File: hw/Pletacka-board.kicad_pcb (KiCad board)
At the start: 2 copper layers, 12 parts, among them SW1 SW_Push_Dual_x2, SW2 SW_Push_Dual_x2, SW3 SW_Push_Dual_x2

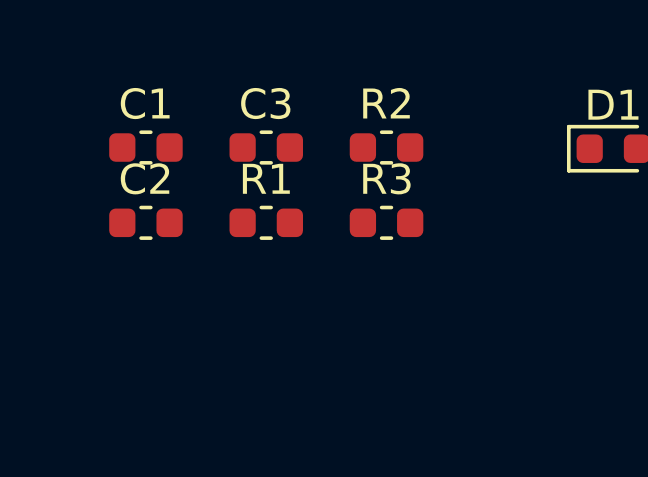
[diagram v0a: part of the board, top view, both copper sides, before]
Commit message: Add octocoupler library
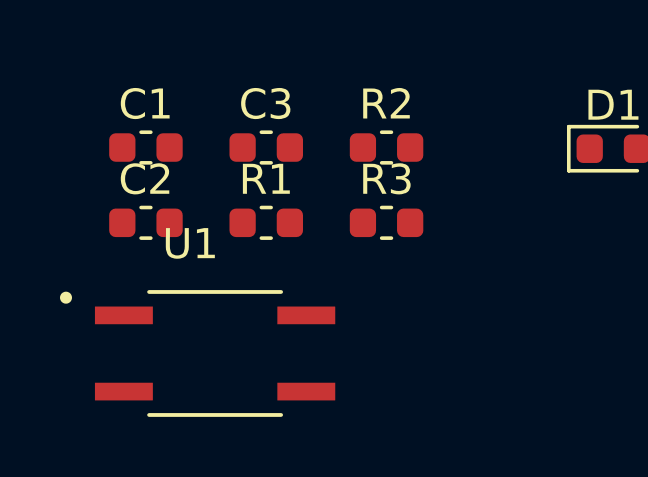
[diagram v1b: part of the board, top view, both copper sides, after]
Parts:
- added U1: EL357N(A)(TA)-G, EL357N_A__TA_-G:SOP254P700X200-4N, F.Cu at (-304.8, -236.2)
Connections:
- E1 pad 12: (no net) -> Net-(E1-Pad12)
- E1 pad 13: (no net) -> Net-(E1-Pad13)
- E1 pad 15: (no net) -> Net-(E1-Pad15)
- E1 pad 17: (no net) -> Net-(E1-Pad17)
- E1 pad 2: (no net) -> Net-(E1-Pad2)
- E1 pad 21: (no net) -> Net-(E1-Pad21)
- E1 pad 22: (no net) -> Net-(E1-Pad22)
- E1 pad 25: (no net) -> Net-(E1-Pad25)
- E1 pad 26: (no net) -> Net-(E1-Pad26)
- E1 pad 27: (no net) -> Net-(E1-Pad27)
- E1 pad 32: (no net) -> Net-(E1-Pad32)
- E1 pad 33: (no net) -> Net-(E1-Pad33)
- E1 pad 36: (no net) -> Net-(E1-Pad36)
- E1 pad 37: (no net) -> Net-(E1-Pad37)
- E1 pad 38: (no net) -> Net-(E1-Pad38)
- E1 pad 39: (no net) -> Net-(E1-Pad39)
- E1 pad 5V: (no net) -> +5V
- R1 pad 1: (no net) -> BTN_RESET
- R2 pad 1: (no net) -> BTN_1
- R3 pad 1: (no net) -> BTN_2
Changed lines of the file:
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@@
     (tracks 0)
     (zones 0)
-    (modules 12)
-    (nets 7)
+    (modules 13)
+    (nets 31)
   )
   (page A4)
@@
   (net 5 "Net-(C2-Pad1)")
   (net 6 "Net-(D1-Pad2)")
+  (net 7 "Net-(E1-Pad12)")
+  (net 8 "Net-(E1-Pad13)")
+  (net 9 "Net-(E1-Pad15)")
+  (net 10 "Net-(E1-Pad2)")
+  (net 11 "Net-(E1-Pad17)")
+  (net 12 "Net-(E1-Pad22)")
+  (net 13 "Net-(E1-Pad21)")
+  (net 14 +5V)
+  (net 15 "Net-(E1-Pad27)")
+  (net 16 "Net-(E1-Pad26)")
+  (net 17 "Net-(E1-Pad25)")
+  (net 18 "Net-(E1-Pad33)")
+  (net 19 "Net-(E1-Pad32)")
+  (net 20 "Net-(E1-Pad39)")
+  (net 21 "Net-(E1-Pad38)")
+  (net 22 "Net-(E1-Pad37)")
+  (net 23 "Net-(E1-Pad36)")
+  (net 24 BTN_RESET)
+  (net 25 BTN_1)
+  (net 26 BTN_2)
+  (net 27 "Net-(U1-Pad1)")
+  (net 28 "Net-(U1-Pad2)")
+  (net 29 "Net-(U1-Pad3)")
+  (net 30 "Net-(U1-Pad4)")
   (net_class Default "This is the default net class."
     (clearance 0.2)
@@
     (uvia_drill 0.1)
     (add_net +3V3)
+    (add_net +5V)
     (add_net BTN_1)
     (add_net BTN_2)
+    (add_net BTN_RESET)
     (add_net GND)
     (add_net "Net-(C1-Pad1)")
@@
     (add_net "Net-(C3-Pad1)")
     (add_net "Net-(D1-Pad2)")
+    (add_net "Net-(E1-Pad12)")
+    (add_net "Net-(E1-Pad13)")
+    (add_net "Net-(E1-Pad15)")
+    (add_net "Net-(E1-Pad17)")
+    (add_net "Net-(E1-Pad2)")
+    (add_net "Net-(E1-Pad21)")
+    (add_net "Net-(E1-Pad22)")
+    (add_net "Net-(E1-Pad25)")
+    (add_net "Net-(E1-Pad26)")
+    (add_net "Net-(E1-Pad27)")
+    (add_net "Net-(E1-Pad32)")
+    (add_net "Net-(E1-Pad33)")
+    (add_net "Net-(E1-Pad36)")
+    (add_net "Net-(E1-Pad37)")
+    (add_net "Net-(E1-Pad38)")
+    (add_net "Net-(E1-Pad39)")
+    (add_net "Net-(U1-Pad1)")
+    (add_net "Net-(U1-Pad2)")
+    (add_net "Net-(U1-Pad3)")
+    (add_net "Net-(U1-Pad4)")
+  )
+  (module EL357N_A__TA_-G:SOP254P700X200-4N (layer F.Cu)
+    (at -304.8 -236.22)
+    (fp_text reference U1 (at -0.82154 -3.64071) (layer F.SilkS)
+      (effects (font (size 1.002756 1.002756) (thickness 0.015)))
+    )
+    (fp_text value "EL357N(A)(TA)-G" (at 6.80906 3.64082) (layer F.Fab)
+      (effects (font (size 1.001874 1.001874) (thickness 0.015)))
+    )
+    (fp_circle (center -4.97 -1.86) (end -4.87 -1.86) (layer F.SilkS) (width 0.2))
+    (fp_circle (center -4.97 -1.86) (end -4.87 -1.86) (layer F.Fab) (width 0.2))
+    (fp_line (start -2.2 -2.05) (end 2.2 -2.05) (layer F.Fab) (width 0.127))
+    (fp_line (start -2.2 2.05) (end 2.2 2.05) (layer F.Fab) (width 0.127))
+    (fp_line (start -2.2 -2.05) (end 2.2 -2.05) (layer F.SilkS) (width 0.127))
+    (fp_line (start -2.2 2.05) (end 2.2 2.05) (layer F.SilkS) (width 0.127))
+    (fp_line (start -2.2 -2.05) (end -2.2 2.05) (layer F.Fab) (width 0.127))
+    (fp_line (start 2.2 -2.05) (end 2.2 2.05) (layer F.Fab) (width 0.127))
+    (fp_line (start -4.255 -2.3) (end 4.255 -2.3) (layer F.CrtYd) (width 0.05))
+    (fp_line (start -4.255 2.3) (end 4.255 2.3) (layer F.CrtYd) (width 0.05))
+    (fp_line (start -4.255 -2.3) (end -4.255 2.3) (layer F.CrtYd) (width 0.05))
+    (fp_line (start 4.255 -2.3) (end 4.255 2.3) (layer F.CrtYd) (width 0.05))
+    (pad 1 smd rect (at -3.04 -1.27) (size 1.93 0.59) (layers F.Cu F.Paste F.Mask)
+      (net 27 "Net-(U1-Pad1)"))
+    (pad 2 smd rect (at -3.04 1.27) (size 1.93 0.59) (layers F.Cu F.Paste F.Mask)
+      (net 28 "Net-(U1-Pad2)"))
+    (pad 3 smd rect (at 3.04 1.27) (size 1.93 0.59) (layers F.Cu F.Paste F.Mask)
+      (net 29 "Net-(U1-Pad3)"))
+    (pad 4 smd rect (at 3.04 -1.27) (size 1.93 0.59) (layers F.Cu F.Paste F.Mask)
+      (net 30 "Net-(U1-Pad4)"))
   )
   (module Resistor_SMD:R_0603_1608Metric (layer F.Cu)
@@
     (pad 2 smd roundrect (at 0.7875 0) (size 0.875 0.95) (layers F.Cu F.Paste F.Mask) (roundrect_rratio 0.25)
       (net 4 "Net-(C3-Pad1)"))
-    (pad 1 smd roundrect (at -0.7875 0) (size 0.875 0.95) (layers F.Cu F.Paste F.Mask) (roundrect_rratio 0.25))
+    (pad 1 smd roundrect (at -0.7875 0) (size 0.875 0.95) (layers F.Cu F.Paste F.Mask) (roundrect_rratio 0.25)
+      (net 26 BTN_2))
     (model ${KISYS3DMOD}/Resistor_SMD.3dshapes/R_0603_1608Metric.wrl
       (at (xyz 0 0 0))
@@
     (pad 2 smd roundrect (at 0.7875 0) (size 0.875 0.95) (layers F.Cu F.Paste F.Mask) (roundrect_rratio 0.25)
       (net 5 "Net-(C2-Pad1)"))
-    (pad 1 smd roundrect (at -0.7875 0) (size 0.875 0.95) (layers F.Cu F.Paste F.Mask) (roundrect_rratio 0.25))
+    (pad 1 smd roundrect (at -0.7875 0) (size 0.875 0.95) (layers F.Cu F.Paste F.Mask) (roundrect_rratio 0.25)
+      (net 25 BTN_1))
     (model ${KISYS3DMOD}/Resistor_SMD.3dshapes/R_0603_1608Metric.wrl
       (at (xyz 0 0 0))
@@
     (pad 2 smd roundrect (at 0.7875 0) (size 0.875 0.95) (layers F.Cu F.Paste F.Mask) (roundrect_rratio 0.25)
       (net 3 "Net-(C1-Pad1)"))
-    (pad 1 smd roundrect (at -0.7875 0) (size 0.875 0.95) (layers F.Cu F.Paste F.Mask) (roundrect_rratio 0.25))
+    (pad 1 smd roundrect (at -0.7875 0) (size 0.875 0.95) (layers F.Cu F.Paste F.Mask) (roundrect_rratio 0.25)
+      (net 24 BTN_RESET))
     (model ${KISYS3DMOD}/Resistor_SMD.3dshapes/R_0603_1608Metric.wrl
       (at (xyz 0 0 0))
@@
     (pad G3 thru_hole circle (at -11.43 5.08) (size 1.524 1.524) (drill 0.762) (layers *.Cu *.Mask)
       (net 2 GND))
-    (pad 12 thru_hole circle (at -11.43 2.54) (size 1.524 1.524) (drill 0.762) (layers *.Cu *.Mask))
-    (pad 13 thru_hole circle (at -11.43 0) (size 1.524 1.524) (drill 0.762) (layers *.Cu *.Mask))
-    (pad 15 thru_hole circle (at -11.43 -2.54) (size 1.524 1.524) (drill 0.762) (layers *.Cu *.Mask))
-    (pad 2 thru_hole circle (at -11.43 -5.08) (size 1.524 1.524) (drill 0.762) (layers *.Cu *.Mask))
-    (pad 17 thru_hole circle (at -11.43 -7.62) (size 1.524 1.524) (drill 0.762) (layers *.Cu *.Mask))
-    (pad 22 thru_hole circle (at -11.43 -10.16) (size 1.524 1.524) (drill 0.762) (layers *.Cu *.Mask))
-    (pad 21 thru_hole circle (at -11.43 -12.7) (size 1.524 1.524) (drill 0.762) (layers *.Cu *.Mask))
+    (pad 12 thru_hole circle (at -11.43 2.54) (size 1.524 1.524) (drill 0.762) (layers *.Cu *.Mask)
+      (net 7 "Net-(E1-Pad12)"))
+    (pad 13 thru_hole circle (at -11.43 0) (size 1.524 1.524) (drill 0.762) (layers *.Cu *.Mask)
+      (net 8 "Net-(E1-Pad13)"))
+    (pad 15 thru_hole circle (at -11.43 -2.54) (size 1.524 1.524) (drill 0.762) (layers *.Cu *.Mask)
+      (net 9 "Net-(E1-Pad15)"))
+    (pad 2 thru_hole circle (at -11.43 -5.08) (size 1.524 1.524) (drill 0.762) (layers *.Cu *.Mask)
+      (net 10 "Net-(E1-Pad2)"))
+    (pad 17 thru_hole circle (at -11.43 -7.62) (size 1.524 1.524) (drill 0.762) (layers *.Cu *.Mask)
+      (net 11 "Net-(E1-Pad17)"))
+    (pad 22 thru_hole circle (at -11.43 -10.16) (size 1.524 1.524) (drill 0.762) (layers *.Cu *.Mask)
+      (net 12 "Net-(E1-Pad22)"))
+    (pad 21 thru_hole circle (at -11.43 -12.7) (size 1.524 1.524) (drill 0.762) (layers *.Cu *.Mask)
+      (net 13 "Net-(E1-Pad21)"))
     (pad G2 thru_hole circle (at -11.43 -15.24) (size 1.524 1.524) (drill 0.762) (layers *.Cu *.Mask)
       (net 2 GND))
     (pad G1 thru_hole circle (at -11.43 -17.78) (size 1.524 1.524) (drill 0.762) (layers *.Cu *.Mask)
       (net 2 GND))
-    (pad 5V thru_hole circle (at 11.43 10.16) (size 1.524 1.524) (drill 0.762) (layers *.Cu *.Mask))
+    (pad 5V thru_hole circle (at 11.43 10.16) (size 1.524 1.524) (drill 0.762) (layers *.Cu *.Mask)
+      (net 14 +5V))
     (pad G5 thru_hole circle (at 11.43 7.62) (size 1.524 1.524) (drill 0.762) (layers *.Cu *.Mask)
       (net 2 GND))
-    (pad 27 thru_hole circle (at 11.43 5.08) (size 1.524 1.524) (drill 0.762) (layers *.Cu *.Mask))
-    (pad 26 thru_hole circle (at 11.43 2.54) (size 1.524 1.524) (drill 0.762) (layers *.Cu *.Mask))
-    (pad 25 thru_hole circle (at 11.43 0) (size 1.524 1.524) (drill 0.762) (layers *.Cu *.Mask))
-    (pad 33 thru_hole circle (at 11.43 -2.54) (size 1.524 1.524) (drill 0.762) (layers *.Cu *.Mask))
-    (pad 32 thru_hole circle (at 11.43 -5.08) (size 1.524 1.524) (drill 0.762) (layers *.Cu *.Mask))
-    (pad 39 thru_hole circle (at 11.43 -7.62) (size 1.524 1.524) (drill 0.762) (layers *.Cu *.Mask))
-    (pad 38 thru_hole circle (at 11.43 -10.16) (size 1.524 1.524) (drill 0.762) (layers *.Cu *.Mask))
-    (pad 37 thru_hole circle (at 11.43 -12.7) (size 1.524 1.524) (drill 0.762) (layers *.Cu *.Mask))
-    (pad 36 thru_hole circle (at 11.43 -15.24) (size 1.524 1.524) (drill 0.762) (layers *.Cu *.Mask))
+    (pad 27 thru_hole circle (at 11.43 5.08) (size 1.524 1.524) (drill 0.762) (layers *.Cu *.Mask)
+      (net 15 "Net-(E1-Pad27)"))
+    (pad 26 thru_hole circle (at 11.43 2.54) (size 1.524 1.524) (drill 0.762) (layers *.Cu *.Mask)
+      (net 16 "Net-(E1-Pad26)"))
+    (pad 25 thru_hole circle (at 11.43 0) (size 1.524 1.524) (drill 0.762) (layers *.Cu *.Mask)
+      (net 17 "Net-(E1-Pad25)"))
+    (pad 33 thru_hole circle (at 11.43 -2.54) (size 1.524 1.524) (drill 0.762) (layers *.Cu *.Mask)
+      (net 18 "Net-(E1-Pad33)"))
+    (pad 32 thru_hole circle (at 11.43 -5.08) (size 1.524 1.524) (drill 0.762) (layers *.Cu *.Mask)
+      (net 19 "Net-(E1-Pad32)"))
+    (pad 39 thru_hole circle (at 11.43 -7.62) (size 1.524 1.524) (drill 0.762) (layers *.Cu *.Mask)
+      (net 20 "Net-(E1-Pad39)"))
+    (pad 38 thru_hole circle (at 11.43 -10.16) (size 1.524 1.524) (drill 0.762) (layers *.Cu *.Mask)
+      (net 21 "Net-(E1-Pad38)"))
+    (pad 37 thru_hole circle (at 11.43 -12.7) (size 1.524 1.524) (drill 0.762) (layers *.Cu *.Mask)
+      (net 22 "Net-(E1-Pad37)"))
+    (pad 36 thru_hole circle (at 11.43 -15.24) (size 1.524 1.524) (drill 0.762) (layers *.Cu *.Mask)
+      (net 23 "Net-(E1-Pad36)"))
     (pad 3V3-2 thru_hole circle (at 11.43 -17.78) (size 1.524 1.524) (drill 0.762) (layers *.Cu *.Mask)
       (net 1 +3V3))

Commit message: Add libraries
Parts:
- added D2: B5819W, B5819W:B5819W_SOD-123, F.Cu at (148.6, 137.2)
- added U2: EL357N(A)(TA)-G, EL357N_A__TA_-G:SOP254P700X200-4N, F.Cu at (118.2, 232.2)
- moved E1 787.0 mm to (100.4, 105.5)
- moved SW3 786.4 mm to (188.7, 87.6)
- moved SW2 773.3 mm to (170.2, 76.2)
- moved SW1 770.7 mm to (146.1, 76.2)
- moved C1 608.4 mm to (200.2, 92.7)
- moved U1 594.9 mm to (166.4, 127.0)
- moved C2 579.8 mm to (148.8, 117.6)
- moved C3 579.8 mm to (152.8, 115.1)
- moved R1 579.8 mm to (152.8, 117.6)
- moved R2 579.8 mm to (156.8, 115.1)
- moved R3 579.8 mm to (156.8, 117.6)
- moved D1 536.2 mm to (129.5, 88.9), turned to 180 degrees
- moved R4 530.1 mm to (125.7, 88.9), turned to 180 degrees
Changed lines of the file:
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@@
     (tracks 0)
     (zones 0)
-    (modules 13)
-    (nets 31)
+    (modules 15)
+    (nets 37)
   )
   (page A4)
@@
   (net 29 "Net-(U1-Pad3)")
   (net 30 "Net-(U1-Pad4)")
+  (net 31 "Net-(U2-Pad1)")
+  (net 32 "Net-(U2-Pad2)")
+  (net 33 "Net-(U2-Pad3)")
+  (net 34 "Net-(U2-Pad4)")
+  (net 35 "Net-(D2-PadC)")
+  (net 36 "Net-(D2-PadA)")
   (net_class Default "This is the default net class."
     (clearance 0.2)
@@
     (add_net "Net-(C3-Pad1)")
     (add_net "Net-(D1-Pad2)")
+    (add_net "Net-(D2-PadA)")
+    (add_net "Net-(D2-PadC)")
     (add_net "Net-(E1-Pad12)")
     (add_net "Net-(E1-Pad13)")
@@
     (add_net "Net-(U1-Pad3)")
     (add_net "Net-(U1-Pad4)")
+    (add_net "Net-(U2-Pad1)")
+    (add_net "Net-(U2-Pad2)")
+    (add_net "Net-(U2-Pad3)")
+    (add_net "Net-(U2-Pad4)")
+  )
+  (module B5819W:B5819W_SOD-123 (layer F.Cu)
+    (at 148.59 137.16)
+    (fp_text reference D2 (at 2.075 -1.635) (layer F.SilkS)
+      (effects (font (size 1 1) (thickness 0.015)))
+    )
+    (fp_text value B5819W (at 3.345 1.665) (layer F.Fab)
+      (effects (font (size 1 1) (thickness 0.015)))
+    )
+    (fp_line (start -1.1 -0.7) (end 1.1 -0.7) (layer F.Fab) (width 0.254))
+    (fp_line (start 1.1 -0.7) (end 1.1 0.7) (layer F.Fab) (width 0.254))
+    (fp_line (start 1.1 0.7) (end -1.1 0.7) (layer F.Fab) (width 0.254))
+    (fp_line (start -1.1 0.7) (end -1.1 -0.7) (layer F.Fab) (width 0.254))
+    (fp_poly (pts (xy -1.95 -0.4) (xy -1.2 -0.4) (xy -1.2 0.45) (xy -1.95 0.45)) (layer F.Fab) (width 0.01))
+    (fp_poly (pts (xy 1.2 -0.4) (xy 1.95 -0.4) (xy 1.95 0.45) (xy 1.2 0.45)) (layer F.Fab) (width 0.01))
+    (fp_poly (pts (xy -1.05 -0.7) (xy -0.15 -0.7) (xy -0.15 0.65) (xy -1.05 0.65)) (layer F.Fab) (width 0.01))
+    (fp_line (start -0.635 -0.635) (end -0.635 0.635) (layer Dwgs.User) (width 0.3048))
+    (pad C smd rect (at -1.9 0) (size 1.4 1.4) (layers F.Cu F.Paste F.Mask)
+      (net 35 "Net-(D2-PadC)"))
+    (pad A smd rect (at 1.9 0) (size 1.4 1.4) (layers F.Cu F.Paste F.Mask)
+      (net 36 "Net-(D2-PadA)"))
   )
   (module EL357N_A__TA_-G:SOP254P700X200-4N (layer F.Cu)
-    (at -304.8 -236.22)
+    (at 118.200001 232.195001)
+    (fp_text reference U2 (at -0.82154 -3.64071) (layer F.SilkS)
+      (effects (font (size 1.002756 1.002756) (thickness 0.015)))
+    )
+    (fp_text value "EL357N(A)(TA)-G" (at 6.80906 3.64082) (layer F.Fab)
+      (effects (font (size 1.001874 1.001874) (thickness 0.015)))
+    )
+    (fp_circle (center -4.97 -1.86) (end -4.87 -1.86) (layer F.SilkS) (width 0.2))
+    (fp_circle (center -4.97 -1.86) (end -4.87 -1.86) (layer F.Fab) (width 0.2))
+    (fp_line (start -2.2 -2.05) (end 2.2 -2.05) (layer F.Fab) (width 0.127))
+    (fp_line (start -2.2 2.05) (end 2.2 2.05) (layer F.Fab) (width 0.127))
+    (fp_line (start -2.2 -2.05) (end 2.2 -2.05) (layer F.SilkS) (width 0.127))
+    (fp_line (start -2.2 2.05) (end 2.2 2.05) (layer F.SilkS) (width 0.127))
+    (fp_line (start -2.2 -2.05) (end -2.2 2.05) (layer F.Fab) (width 0.127))
+    (fp_line (start 2.2 -2.05) (end 2.2 2.05) (layer F.Fab) (width 0.127))
+    (fp_line (start -4.255 -2.3) (end 4.255 -2.3) (layer F.CrtYd) (width 0.05))
+    (fp_line (start -4.255 2.3) (end 4.255 2.3) (layer F.CrtYd) (width 0.05))
+    (fp_line (start -4.255 -2.3) (end -4.255 2.3) (layer F.CrtYd) (width 0.05))
+    (fp_line (start 4.255 -2.3) (end 4.255 2.3) (layer F.CrtYd) (width 0.05))
+    (pad 1 smd rect (at -3.04 -1.27) (size 1.93 0.59) (layers F.Cu F.Paste F.Mask)
+      (net 31 "Net-(U2-Pad1)"))
+    (pad 2 smd rect (at -3.04 1.27) (size 1.93 0.59) (layers F.Cu F.Paste F.Mask)
+      (net 32 "Net-(U2-Pad2)"))
+    (pad 3 smd rect (at 3.04 1.27) (size 1.93 0.59) (layers F.Cu F.Paste F.Mask)
+      (net 33 "Net-(U2-Pad3)"))
+    (pad 4 smd rect (at 3.04 -1.27) (size 1.93 0.59) (layers F.Cu F.Paste F.Mask)
+      (net 34 "Net-(U2-Pad4)"))
+  )
+  (module EL357N_A__TA_-G:SOP254P700X200-4N (layer F.Cu)
+    (at 166.37 127)
     (fp_text reference U1 (at -0.82154 -3.64071) (layer F.SilkS)
       (effects (font (size 1.002756 1.002756) (thickness 0.015)))
@@
   )
   (module Resistor_SMD:R_0603_1608Metric (layer F.Cu)
-    (at -287.514999 -243.084999)
+    (at 125.73 88.9 180)
     (descr "Resistor SMD 0603 (1608 Metric), square (rectangular) end terminal, IPC_7351 nominal, (Body size source: http://www.tortai-tech.com/upload/download/2011102023233369053.pdf), generated with kicad-footprint-generator")
     (tags resistor)
@@
     (fp_line (start -0.8 -0.4) (end 0.8 -0.4) (layer F.Fab) (width 0.1))
     (fp_line (start -0.8 0.4) (end -0.8 -0.4) (layer F.Fab) (width 0.1))
-    (pad 2 smd roundrect (at 0.7875 0) (size 0.875 0.95) (layers F.Cu F.Paste F.Mask) (roundrect_rratio 0.25)
+    (pad 2 smd roundrect (at 0.7875 0 180) (size 0.875 0.95) (layers F.Cu F.Paste F.Mask) (roundrect_rratio 0.25)
       (net 1 +3V3))
-    (pad 1 smd roundrect (at -0.7875 0) (size 0.875 0.95) (layers F.Cu F.Paste F.Mask) (roundrect_rratio 0.25)
+    (pad 1 smd roundrect (at -0.7875 0 180) (size 0.875 0.95) (layers F.Cu F.Paste F.Mask) (roundrect_rratio 0.25)
       (net 6 "Net-(D1-Pad2)"))
     (model ${KISYS3DMOD}/Resistor_SMD.3dshapes/R_0603_1608Metric.wrl
@@
   )
   (module Resistor_SMD:R_0603_1608Metric (layer F.Cu)
-    (at -299.084999 -240.574999)
+    (at 156.845001 117.565001)
     (descr "Resistor SMD 0603 (1608 Metric), square (rectangular) end terminal, IPC_7351 nominal, (Body size source: http://www.tortai-tech.com/upload/download/2011102023233369053.pdf), generated with kicad-footprint-generator")
     (tags resistor)
@@
   )
   (module Resistor_SMD:R_0603_1608Metric (layer F.Cu)
-    (at -299.084999 -243.084999)
+    (at 156.845001 115.055001)
     (descr "Resistor SMD 0603 (1608 Metric), square (rectangular) end terminal, IPC_7351 nominal, (Body size source: http://www.tortai-tech.com/upload/download/2011102023233369053.pdf), generated with kicad-footprint-generator")
     (tags resistor)
@@
   )
   (module Resistor_SMD:R_0603_1608Metric (layer F.Cu)
-    (at -303.094999 -240.574999)
+    (at 152.835001 117.565001)
     (descr "Resistor SMD 0603 (1608 Metric), square (rectangular) end terminal, IPC_7351 nominal, (Body size source: http://www.tortai-tech.com/upload/download/2011102023233369053.pdf), generated with kicad-footprint-generator")
     (tags resistor)
@@
   )
   (module LED_SMD:LED_0603_1608Metric (layer F.Cu)
-    (at -291.524999 -243.044999)
+    (at 129.54 88.9 180)
     (descr "LED SMD 0603 (1608 Metric), square (rectangular) end terminal, IPC_7351 nominal, (Body size source: http://www.tortai-tech.com/upload/download/2011102023233369053.pdf), generated with kicad-footprint-generator")
     (tags diode)
@@
     (fp_line (start -0.5 -0.4) (end -0.8 -0.1) (layer F.Fab) (width 0.1))
     (fp_line (start 0.8 -0.4) (end -0.5 -0.4) (layer F.Fab) (width 0.1))
-    (pad 2 smd roundrect (at 0.7875 0) (size 0.875 0.95) (layers F.Cu F.Paste F.Mask) (roundrect_rratio 0.25)
+    (pad 2 smd roundrect (at 0.7875 0 180) (size 0.875 0.95) (layers F.Cu F.Paste F.Mask) (roundrect_rratio 0.25)
       (net 6 "Net-(D1-Pad2)"))
-    (pad 1 smd roundrect (at -0.7875 0) (size 0.875 0.95) (layers F.Cu F.Paste F.Mask) (roundrect_rratio 0.25)
+    (pad 1 smd roundrect (at -0.7875 0 180) (size 0.875 0.95) (layers F.Cu F.Paste F.Mask) (roundrect_rratio 0.25)
       (net 2 GND))
     (model ${KISYS3DMOD}/LED_SMD.3dshapes/LED_0603_1608Metric.wrl
@@
   )
   (module Capacitor_SMD:C_0603_1608Metric (layer F.Cu)
-    (at -303.094999 -243.084999)
+    (at 152.835001 115.055001)
     (descr "Capacitor SMD 0603 (1608 Metric), square (rectangular) end terminal, IPC_7351 nominal, (Body size source: http://www.tortai-tech.com/upload/download/2011102023233369053.pdf), generated with kicad-footprint-generator")
     (tags capacitor)
@@
   )
   (module Capacitor_SMD:C_0603_1608Metric (layer F.Cu)
-    (at -307.104999 -240.574999)
+    (at 148.825001 117.565001)
     (descr "Capacitor SMD 0603 (1608 Metric), square (rectangular) end terminal, IPC_7351 nominal, (Body size source: http://www.tortai-tech.com/upload/download/2011102023233369053.pdf), generated with kicad-footprint-generator")
     (tags capacitor)
@@
   )
   (module Capacitor_SMD:C_0603_1608Metric (layer F.Cu)
-    (at -307.104999 -243.084999)
+    (at 200.1775 92.71)
     (descr "Capacitor SMD 0603 (1608 Metric), square (rectangular) end terminal, IPC_7351 nominal, (Body size source: http://www.tortai-tech.com/upload/download/2011102023233369053.pdf), generated with kicad-footprint-generator")
     (tags capacitor)
@@
   )
   (module Resistor_SMD:R_0603_1608Metric (layer F.Cu)
-    (at 10.445001 -678.294999)
+    (at 188.7475 87.63)
     (descr "Resistor SMD 0603 (1608 Metric), square (rectangular) end terminal, IPC_7351 nominal, (Body size source: http://www.tortai-tech.com/upload/download/2011102023233369053.pdf), generated with kicad-footprint-generator")
     (tags resistor)
@@
   )
   (module Button_Switch_SMD:SW_SPST_SKQG_WithStem (layer F.Cu)
-    (at 22.765001 -682.924999)
+    (at 170.18 76.2)
     (descr "ALPS 5.2mm Square Low-profile Type (Surface Mount) SKQG Series, With stem, http://www.alps.com/prod/info/E/HTML/Tact/SurfaceMount/SKQG/SKQGAFE010.html")
     (tags "SPST Button Switch")
@@
   )
   (module Button_Switch_SMD:SW_SPST_SKQG_WithStem (layer F.Cu)
-    (at 13.215001 -682.924999)
+    (at 146.05 76.2)
     (descr "ALPS 5.2mm Square Low-profile Type (Surface Mount) SKQG Series, With stem, http://www.alps.com/prod/info/E/HTML/Tact/SurfaceMount/SKQG/SKQGAFE010.html")
     (tags "SPST Button Switch")
@@
   )
   (module ESP32-TTGO-T-Display:ESP32-TTGO-T-Display (layer F.Cu)
-    (at -81.219999 -660.339999)
+    (at 100.390001 105.470001)
     (fp_text reference E1 (at 7.62 29.21) (layer F.SilkS)
       (effects (font (size 1 1) (thickness 0.15)))
